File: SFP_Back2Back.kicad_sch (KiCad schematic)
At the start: 16 parts, among them J1 Conn_01x04, J101 Barrel_Jack, J2 Conn_01x03, J3 Conn_01x03, U101 LM2576S-3.3

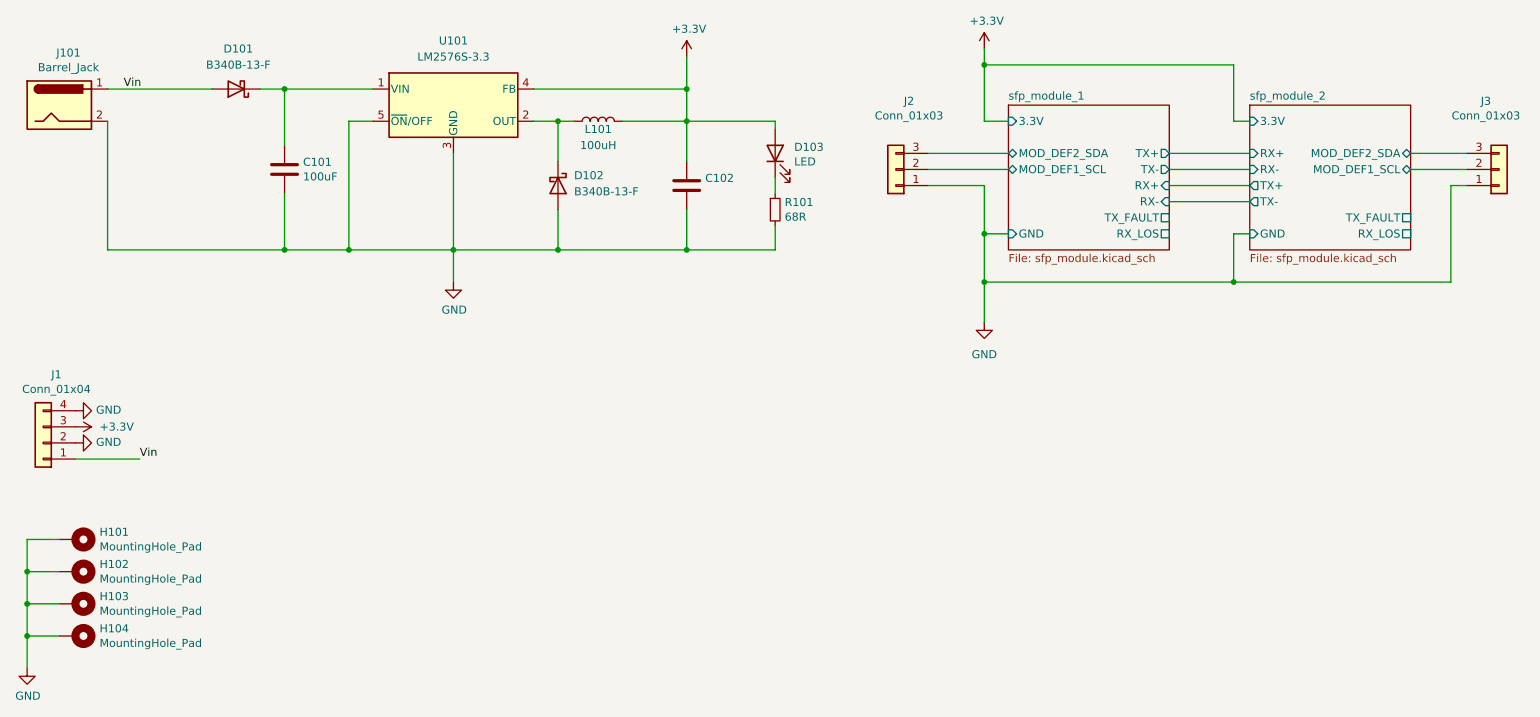
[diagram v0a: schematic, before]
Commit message: Finished PCB and renamed it
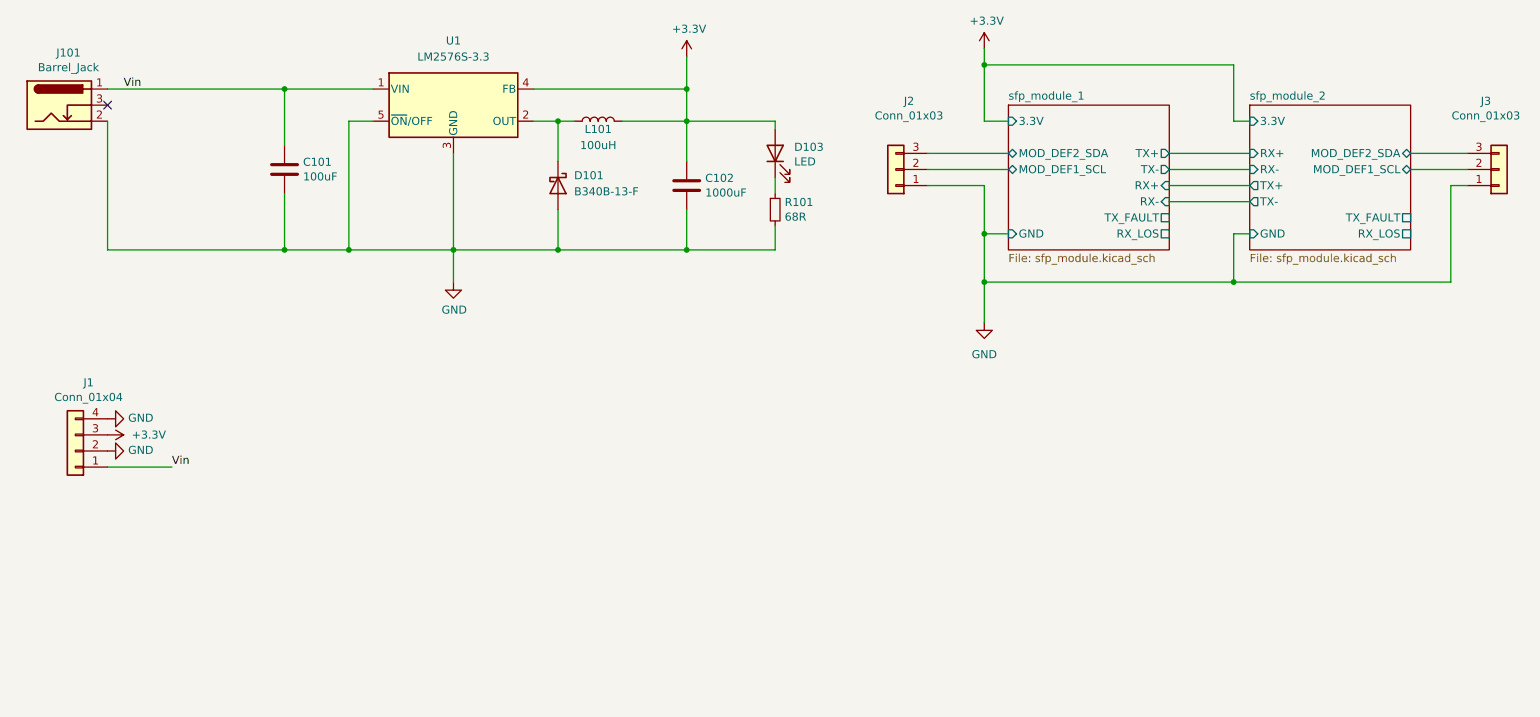
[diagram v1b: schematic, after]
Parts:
- removed D101: B340B-13-F, Diode_SMD:D_SMB, symbol Device:D_Schottky
- removed H101, H102, H103, H104: MountingHole_Pad, symbol Mechanical:MountingHole_Pad
- C101: footprint Capacitor_SMD:CP_Elec_10x10 -> Capacitor_SMD:CP_Elec_6.3x7.7; LCSC C249838 -> (none); LCSC Part Number (none) -> C2992595
- C102: value (none) -> 1000uF; footprint (none) -> Capacitor_SMD:CP_Elec_8x10.5; LCSC Part Number C176684 -> C72471
- J1, J2, J3: now left out of the parts list
- J101: symbol Connector:Barrel_Jack -> Connector:Barrel_Jack_Switch
- renumbered D102 to D101, U101 to U1
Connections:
- net Vin: now also C101.1, U1.1 (VIN)
- no-connect marks 0 -> 1
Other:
- company: (none) -> © foorschtbar
- title: (none) -> SFP Back2Back
- moved on the sheet: J1

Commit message: Fixed Caps Voltage
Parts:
- C101: LCSC Part Number C2992595 -> C72477
- C102: LCSC Part Number C72471 -> C99833
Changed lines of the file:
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@@
       (effects (font (size 1.27 1.27)) hide)
     )
-    (property "LCSC Part Number" "C72471" (id 6) (at 127 91.44 0)
+    (property "LCSC Part Number" "C99833" (id 6) (at 127 91.44 0)
       (effects (font (size 1.27 1.27)) hide)
     )
@@
       (effects (font (size 1.27 1.27)) hide)
     )
-    (property "LCSC Part Number" "C2992595" (id 7) (at 63.5 88.9 0)
+    (property "LCSC Part Number" "C72477" (id 7) (at 63.5 88.9 0)
       (effects (font (size 1.27 1.27)) hide)
     )

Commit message: Fixed LCSC Order Number for 68R Resistor
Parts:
- R101: LCSC Part Number C474219 -> C17802
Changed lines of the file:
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@@
       (effects (font (size 1.27 1.27)) hide)
     )
-    (property "LCSC Part Number" "C474219" (id 4) (at 140.97 95.25 0)
+    (property "LCSC Part Number" "C17802" (id 4) (at 140.97 95.25 0)
       (effects (font (size 1.27 1.27)) hide)
     )
